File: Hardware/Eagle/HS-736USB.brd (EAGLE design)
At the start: 29.9 x 44.4 mm, 10 parts, among them Q1 12Mhz

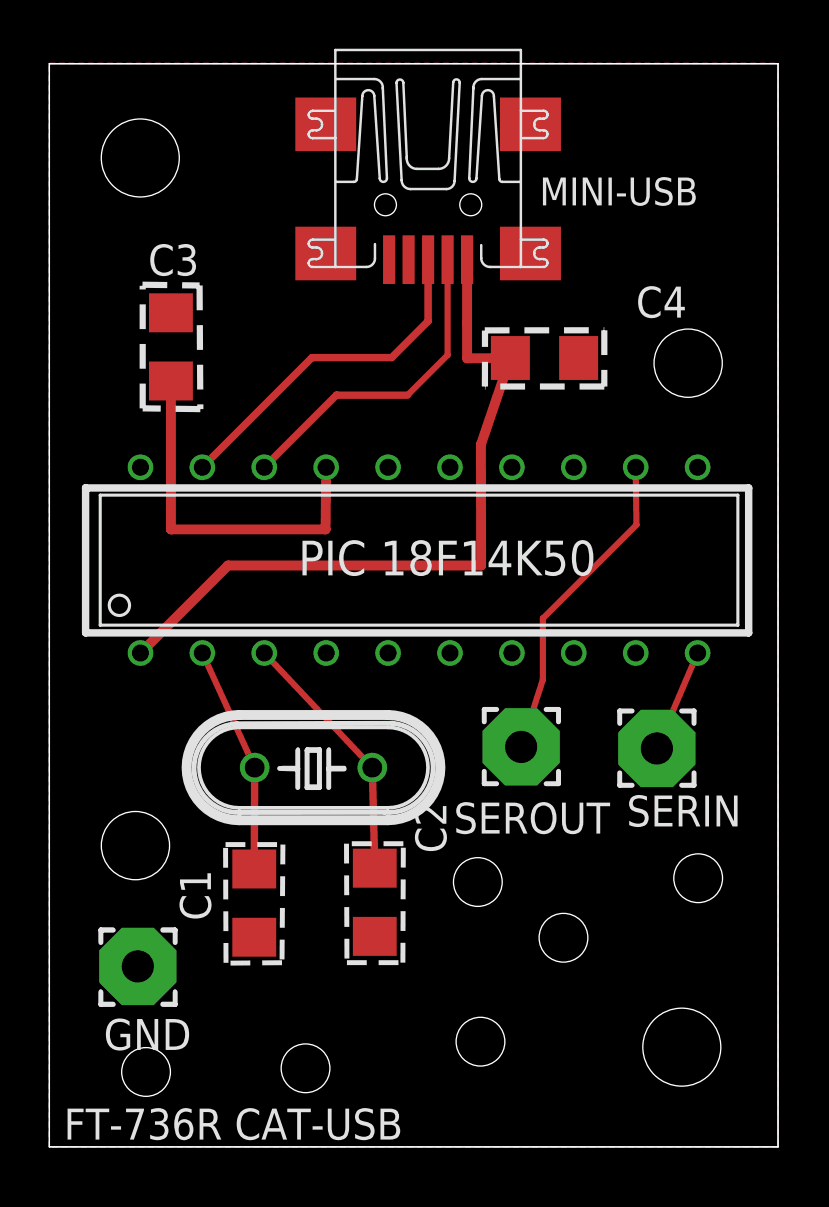
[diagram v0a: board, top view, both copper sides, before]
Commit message: Added USB status LED indicators to the schematic and board layout. Refactored the silkscreen layers to be less cluttered and within boundaries.
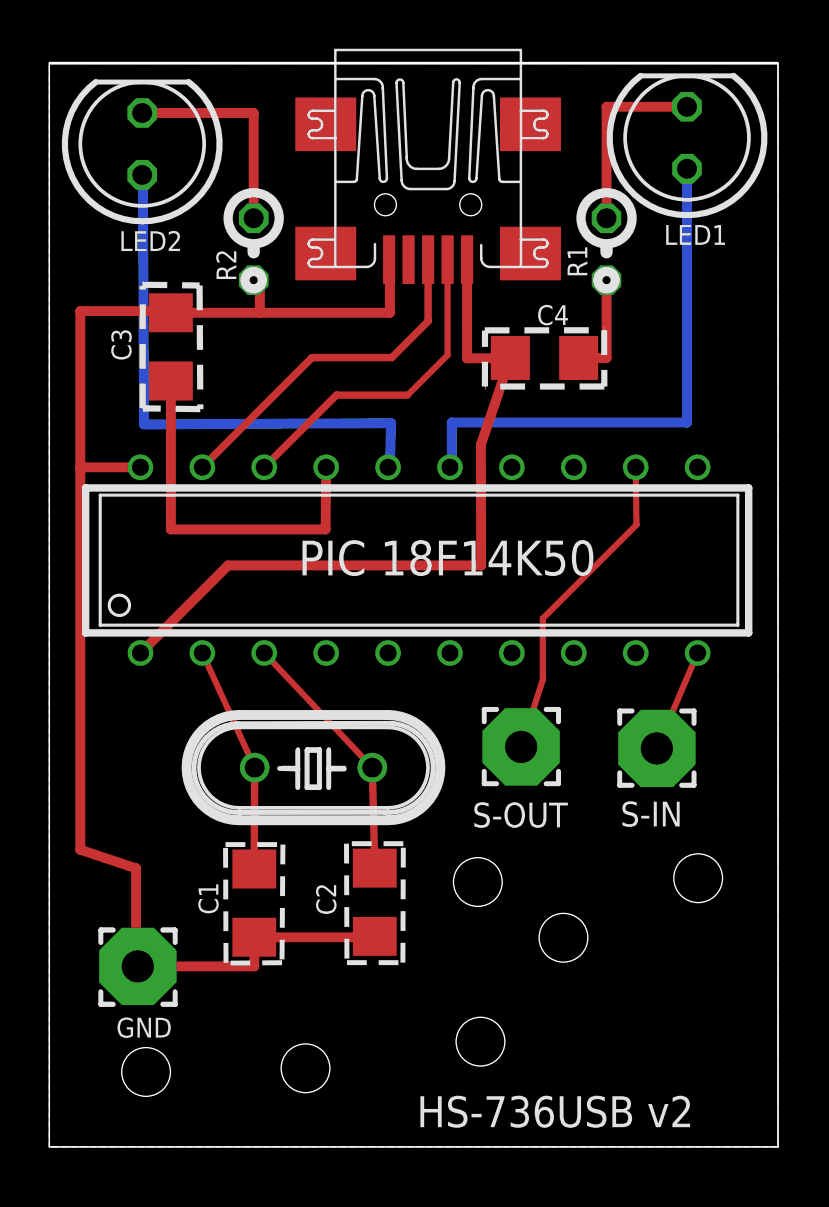
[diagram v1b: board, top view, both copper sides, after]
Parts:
- added LED1, LED2: (no value), led:LED5MM
- added R1, R2: 82Ω, rcl:0204V
- C1, C2: value 22pf -> 22pF
- C3: value .47ufd -> .47µF
- C4: value .1ufd -> .1µF
- Q1: value 12Mhz -> 12MHz
- renumbered SERIN to S-IN, SEROUT to S-OUT
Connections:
- new net N$11: LED2.A, U$1.P$16
- new net N$12: LED1.A, U$1.P$15
- new net N$3: LED2.K, R2.1
- new net N$5: LED1.K, R1.1
- net GND: now also R1.2, R2.2
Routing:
- net GND: track 0.00 -> 61.8 mm
- net N$11: track 0.00 -> 22.3 mm
- net N$12: track 0.00 -> 21.5 mm
- net N$3: track 0.00 -> 8.89 mm
- net N$5: track 0.00 -> 7.87 mm
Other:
- board size 29.9 x 44.4 mm -> 29.9 x 44.5 mm
- board text added: "Copyright 2015 Ham Spot Inc"
- board text added: "HS-736USB v2"
- board text added: "HamSpot.com"
- board text removed: "Copyright 2014 Ham Spot Inc"
- board text removed: "FT-736R CAT-USB"
- board text removed: "MINI-USB"
